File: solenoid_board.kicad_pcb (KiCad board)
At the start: 2 copper layers, 34 parts, among them J2 MCU_LEFT_LEGS, J3 MCU_RIGHT_LEGS

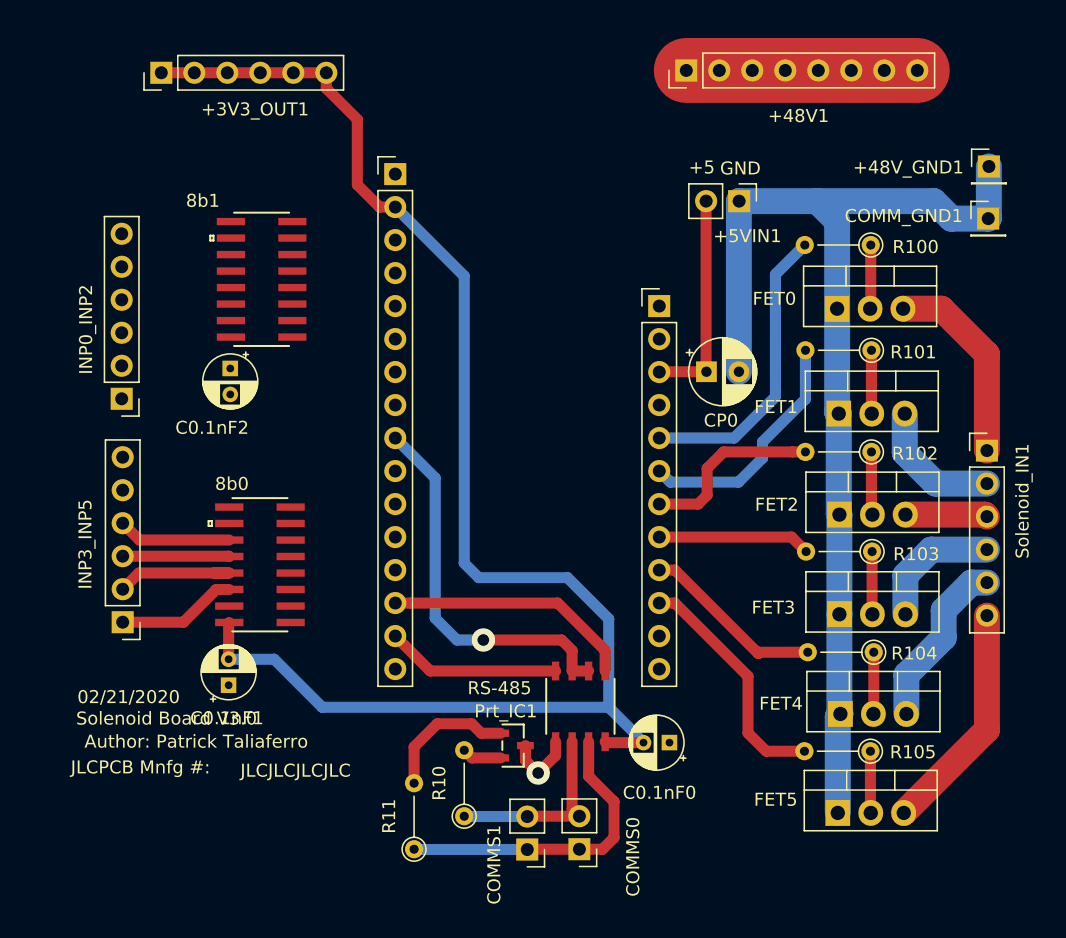
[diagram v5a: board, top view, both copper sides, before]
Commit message: V3 Commit. Screw terminals swapped out for pin headers. Geometry changed. The board is now much smaller.
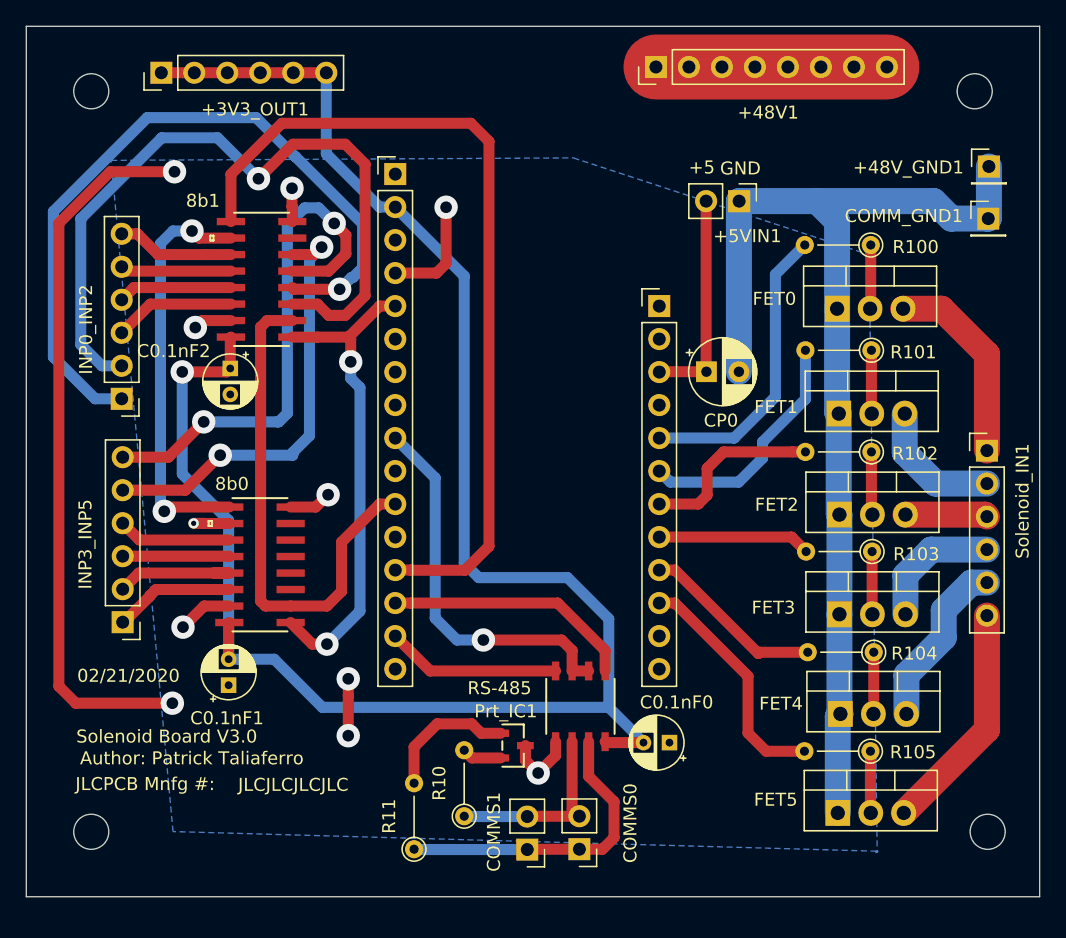
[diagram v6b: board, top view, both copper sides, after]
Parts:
- added REF**: MountingHole_2.7mm_M2.5, MountingHole:MountingHole_2.7mm_M2.5, F.Cu at (170.0, 65.0)
- added REF**: MountingHole_2.7mm_M2.5, MountingHole:MountingHole_2.7mm_M2.5, F.Cu at (102.0, 65.0)
- added REF**: MountingHole_2.7mm_M2.5, MountingHole:MountingHole_2.7mm_M2.5, F.Cu at (171.0, 122.0)
- added REF**: MountingHole_2.7mm_M2.5, MountingHole:MountingHole_2.7mm_M2.5, F.Cu at (102.0, 122.0)
- moved +48V1 2.35 mm to (145.5, 63.1)
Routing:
- net GND: track 90.3 -> 174.5 mm, vias 1 -> 11
- net /MISO: track 0.00 -> 64.9 mm
- net /INP2_0: track 0.00 -> 57.7 mm, vias 0 -> 1
- net /INP2_1: track 0.00 -> 57.5 mm, vias 0 -> 1
- net /INP3_0: track 0.00 -> 40.6 mm, vias 0 -> 2
- net /SCK: track 0.00 -> 39.7 mm
- net /A0: track 0.00 -> 37.4 mm, vias 0 -> 2
- net /INP3_1: track 0.00 -> 33.6 mm, vias 0 -> 2
- net /SHIFT2_OUT: track 0.00 -> 31.4 mm, vias 0 -> 2
- net +3V3: track 116.8 -> 146.7 mm, vias 0 -> 1
- net /INP1_1: track 0.00 -> 9.32 mm
- net /INP0_0: track 0.00 -> 9.07 mm
- net /INP1_0: track 0.00 -> 8.80 mm
- net /INP0_1: track 0.00 -> 8.54 mm
- net /INP5_1: track 9.25 -> 10.3 mm
- added copper zone on B.Cu, net GND
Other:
- board outline added: 78 x 67 mm

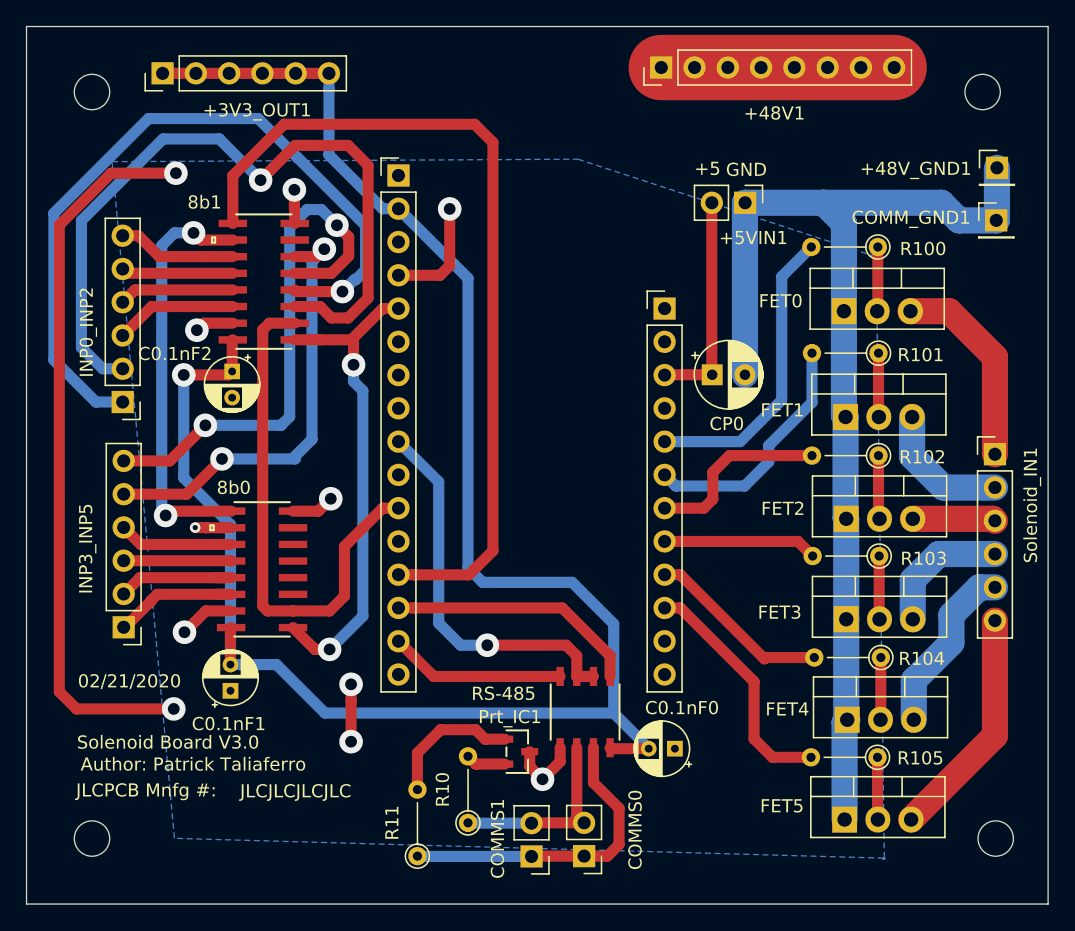
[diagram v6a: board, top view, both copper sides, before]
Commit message: Debugged Solenoid Footprint issue and 3.3V terminal block issue.
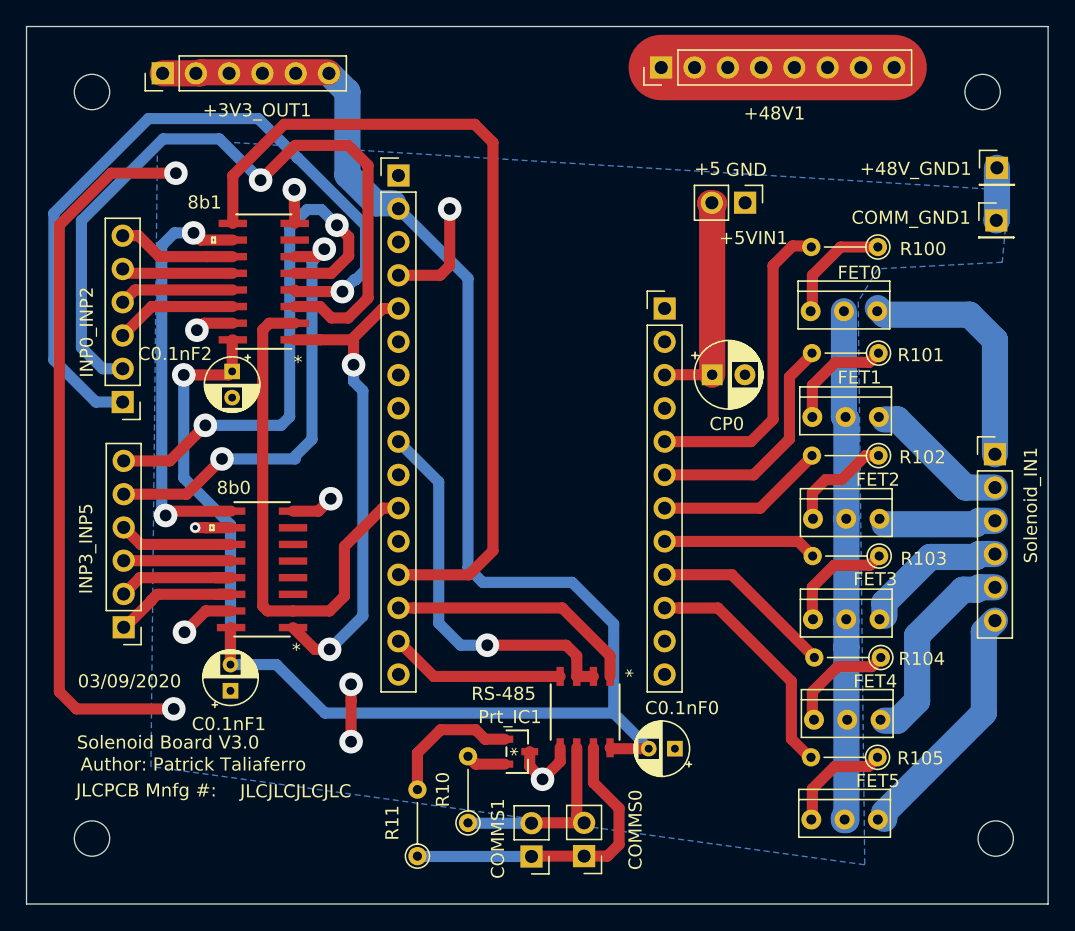
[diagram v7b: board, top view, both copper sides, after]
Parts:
- FET0, FET1, FET2, FET3, FET4, FET5: footprint Package_TO_SOT_THT:TO-220-3_Vertical -> NXP:PHP79NQ08LT,127
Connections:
- 8b0 pad 3: (no net) -> Net-(8b0-Pad3)
- 8b0 pad 4: (no net) -> Net-(8b0-Pad4)
- 8b0 pad 5: (no net) -> Net-(8b0-Pad5)
- 8b0 pad 6: (no net) -> Net-(8b0-Pad6)
- 8b0 pad 7: (no net) -> Net-(8b0-Pad7)
- 8b1 pad 7: (no net) -> Net-(8b1-Pad7)
- J2 pad 1: (no net) -> /RST
- J2 pad 10: (no net) -> /A5
- J2 pad 12: (no net) -> /MOSI
- J2 pad 3: (no net) -> /ARf
- J2 pad 6: (no net) -> /A1
- J2 pad 7: (no net) -> /A2
- J2 pad 8: (no net) -> /A3
- J3 pad 1: (no net) -> /BAT
- J3 pad 11: (no net) -> /SCL
- J3 pad 12: (no net) -> /SDA
- J3 pad 2: (no net) -> /En
- J3 pad 4: (no net) -> /D13
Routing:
- net GND: track 174.5 -> 132.8 mm
- net Net-(FET3-Pad2): track 4.84 -> 8.68 mm
- net Net-(FET0-Pad2): track 4.92 -> 8.75 mm
- net Net-(FET5-Pad2): track 4.76 -> 8.57 mm
- net Net-(FET4-Pad2): track 4.76 -> 8.52 mm
- net Net-(FET1-Pad2): track 4.89 -> 8.47 mm
- net Net-(FET2-Pad2): track 4.86 -> 8.23 mm
- net Net-(FET0-Pad3): track 15.3 -> 18.7 mm
- net Net-(FET2-Pad3): track 6.34 -> 8.55 mm
- net Net-(FET4-Pad3): track 13.4 -> 15.6 mm
- net /D12: track 22.9 -> 24.4 mm
- net /D10: track 14.1 -> 13.1 mm
- net Net-(FET3-Pad3): track 10.1 -> 11.0 mm
- net /D11: track 18.7 -> 17.9 mm
- net Net-(FET5-Pad3): track 17.8 -> 18.6 mm
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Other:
- board text added: "03/09/2020"
- board text removed: "02/21/2020"

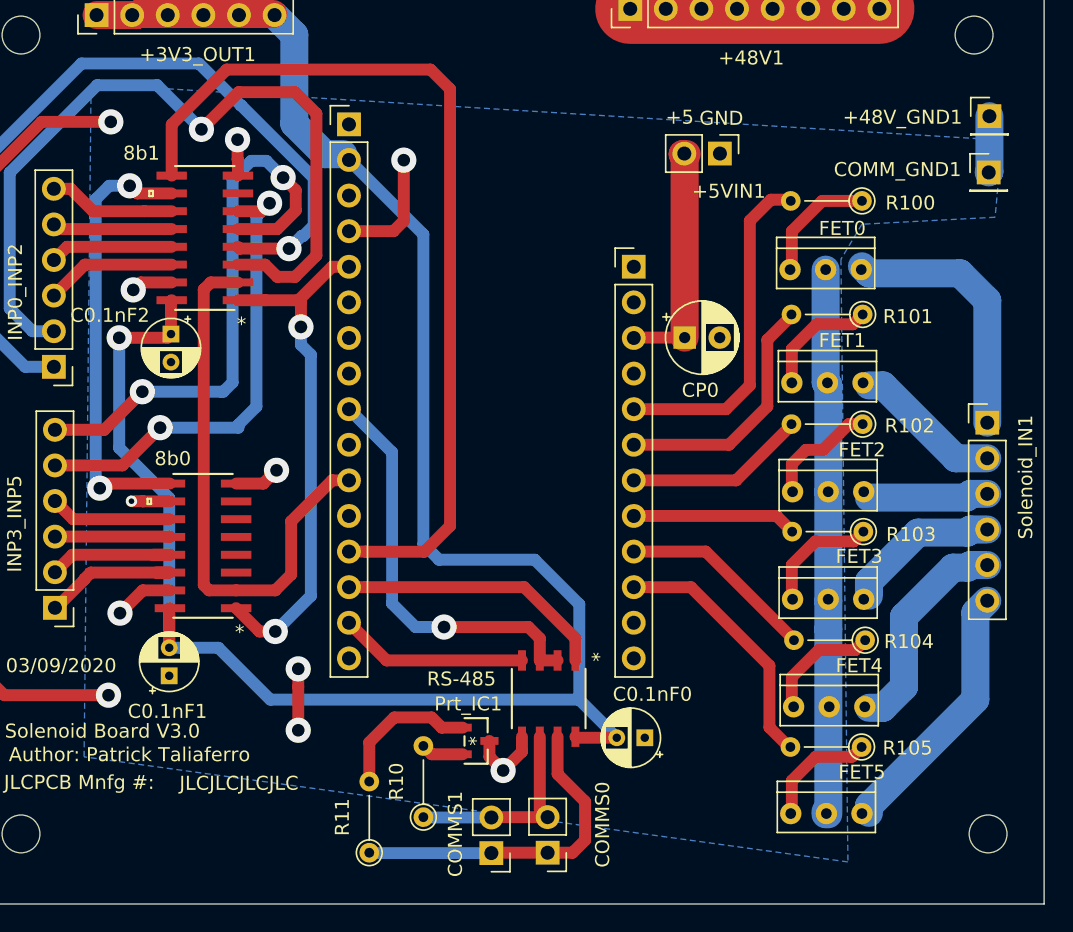
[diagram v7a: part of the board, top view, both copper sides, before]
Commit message: added pull up resistor.
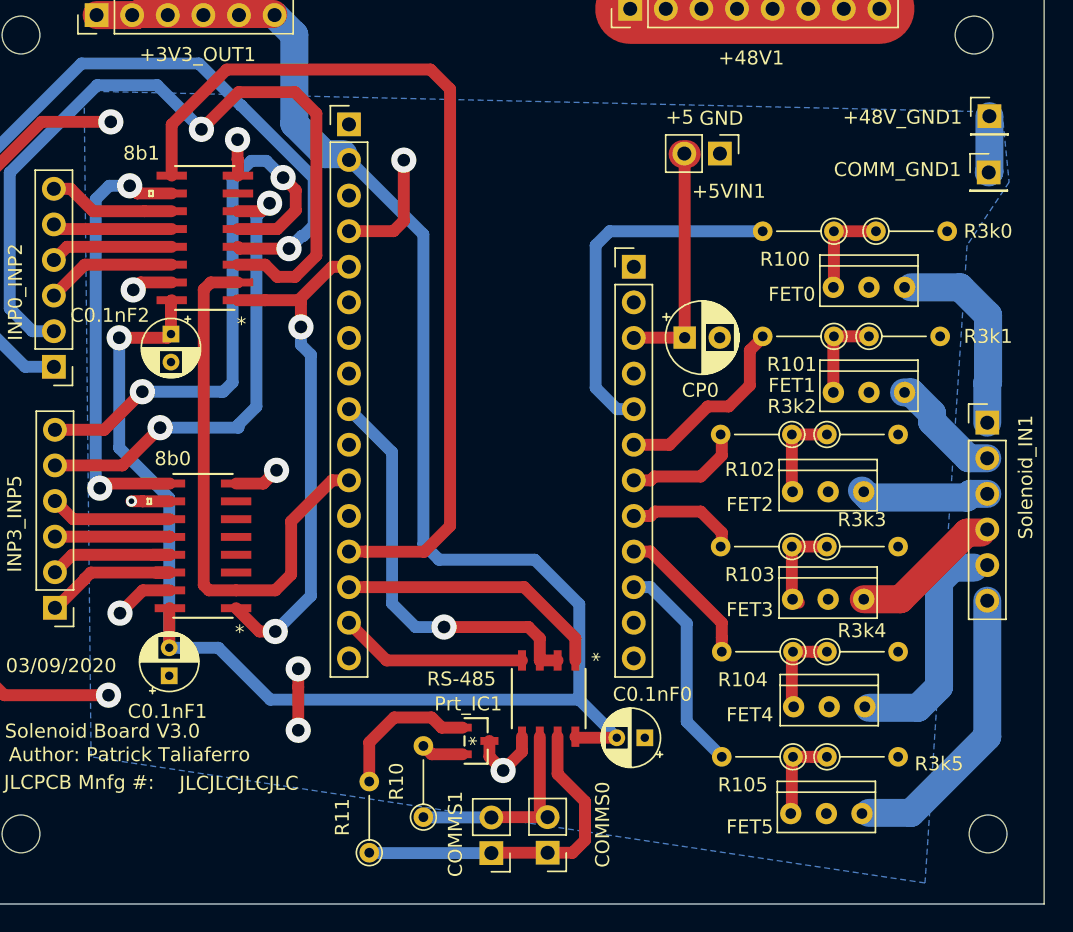
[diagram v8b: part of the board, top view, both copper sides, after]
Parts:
- added R3k0: 3k, Resistor_THT:R_Axial_DIN0204_L3.6mm_D1.6mm_P5.08mm_Vertical, F.Cu at (163.0, 79.0)
- added R3k1: 3k, Resistor_THT:R_Axial_DIN0204_L3.6mm_D1.6mm_P5.08mm_Vertical, F.Cu at (162.5, 86.5)
- added R3k2: 3k, Resistor_THT:R_Axial_DIN0204_L3.6mm_D1.6mm_P5.08mm_Vertical, F.Cu at (159.5, 93.5)
- added R3k3: 3k, Resistor_THT:R_Axial_DIN0204_L3.6mm_D1.6mm_P5.08mm_Vertical, F.Cu at (159.5, 101.5)
- added R3k4: 3k, Resistor_THT:R_Axial_DIN0204_L3.6mm_D1.6mm_P5.08mm_Vertical, F.Cu at (159.5, 109.0)
- added R3k5: 3k, Resistor_THT:R_Axial_DIN0204_L3.6mm_D1.6mm_P5.08mm_Vertical, F.Cu at (159.5, 116.5)
- moved R104 5.21 mm to (157.1, 109.0)
- moved R103 5.21 mm to (157.0, 101.5)
- moved R102 5.11 mm to (157.0, 93.5)
- moved R105 4.95 mm to (157.1, 116.5)
- moved FET0 3.34 mm to (162.5, 83.0)
- moved FET1 3.04 mm to (162.5, 90.5)
- moved R100 2.95 mm to (160.0, 79.0)
- moved R101 2.58 mm to (160.0, 86.5)
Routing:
- net GND: track 132.8 -> 93.7 mm
- net Net-(FET0-Pad3): track 18.7 -> 14.0 mm
- net /D10: track 13.1 -> 8.52 mm
- net /D11: track 17.9 -> 13.9 mm
- net /D9: track 11.7 -> 8.03 mm
- net /D6: track 14.1 -> 10.5 mm
- net /D5: track 18.4 -> 15.4 mm
- net Net-(FET1-Pad3): track 10.6 -> 8.23 mm
- net Net-(FET4-Pad2): track 8.52 -> 6.50 mm
- net Net-(FET1-Pad2): track 8.47 -> 6.52 mm
- net Net-(FET5-Pad2): track 8.57 -> 6.70 mm
- net Net-(FET5-Pad3): track 18.6 -> 20.4 mm
- net Net-(FET0-Pad2): track 8.75 -> 7.00 mm
- net Net-(FET2-Pad2): track 8.23 -> 6.50 mm
- net Net-(FET3-Pad2): track 8.68 -> 7.00 mm
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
